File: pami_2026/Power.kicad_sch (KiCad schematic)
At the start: 6 parts, among them U2 AZ1117CH2-3.3, U3 AZ1117CH2-3.3

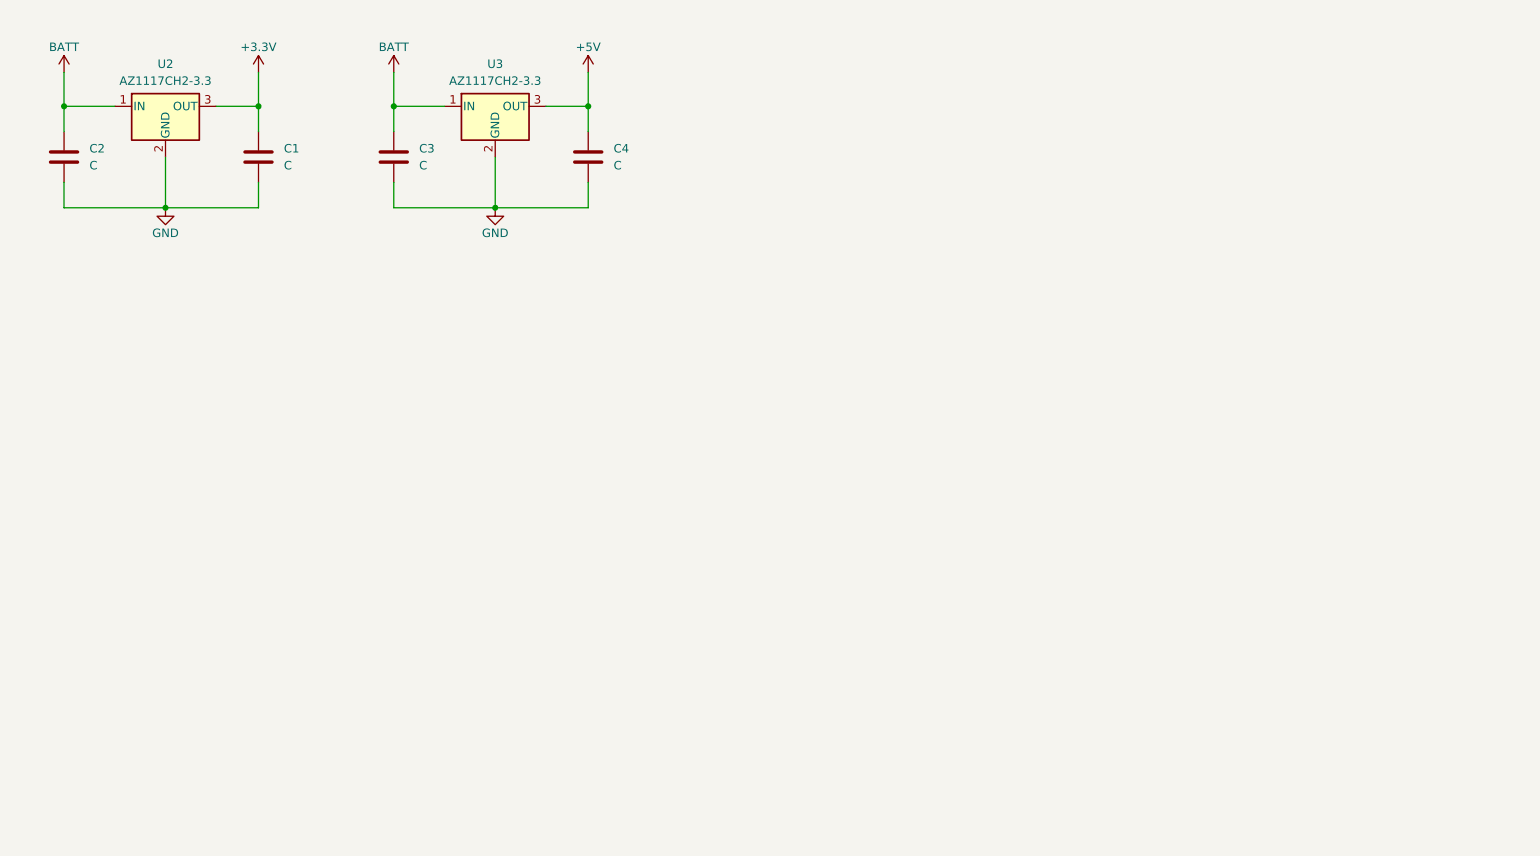
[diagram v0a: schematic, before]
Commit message: Battery circuit and DC Driver
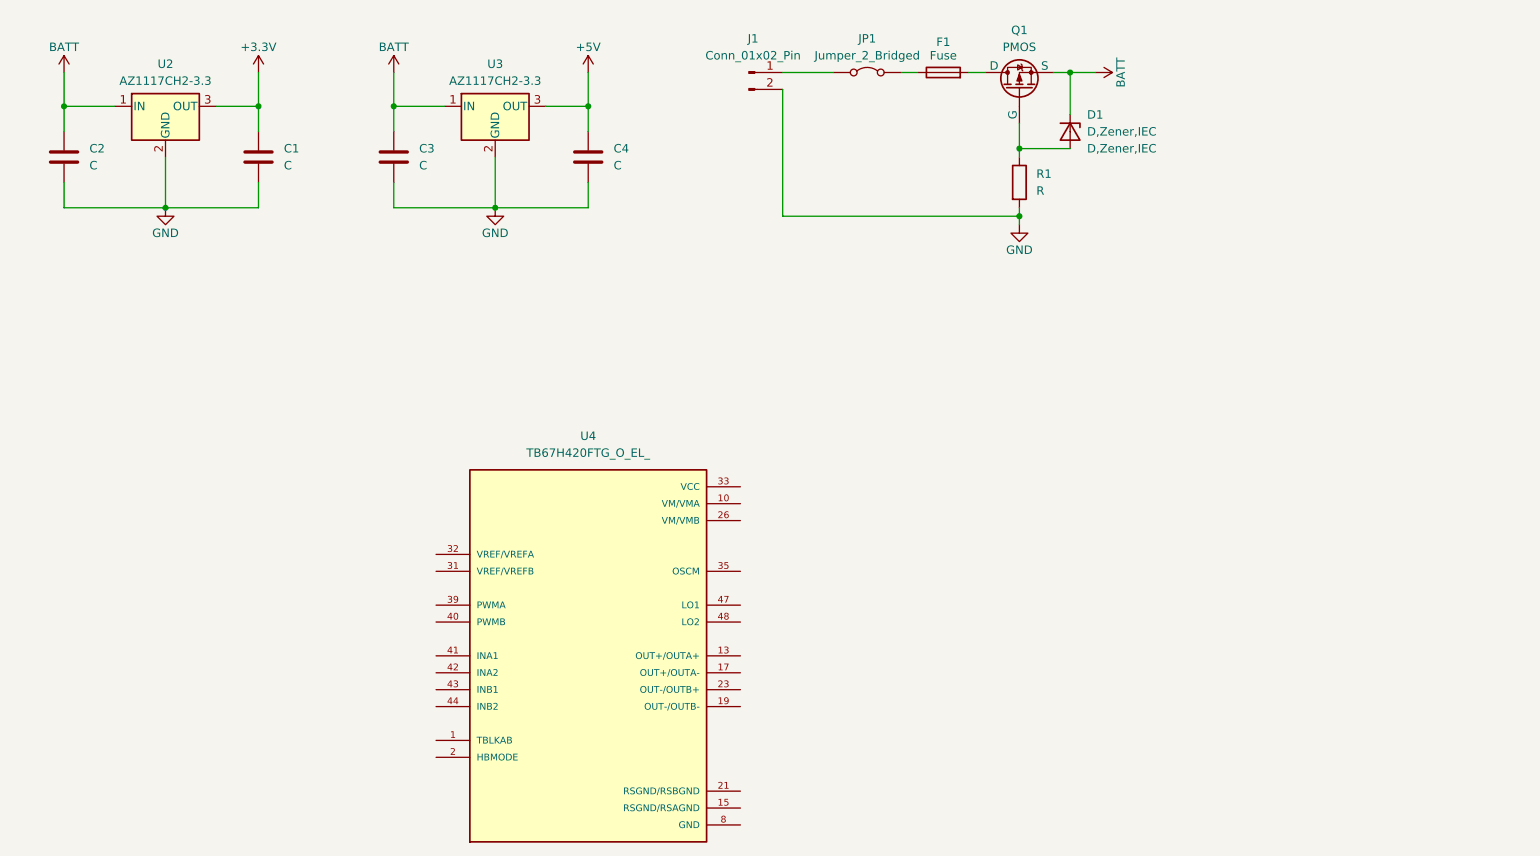
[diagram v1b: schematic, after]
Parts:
- added D1: ${SIM.PARAMS}, symbol PCM_Generic-50:D,Zener,IEC
- added F1: Fuse, symbol Device:Fuse
- added J1: Conn_01x02_Pin, symbol Connector:Conn_01x02_Pin
- added JP1: Jumper_2_Bridged, symbol Jumper:Jumper_2_Bridged
- added Q1: PMOS, symbol Simulation_SPICE:PMOS
- added R1: R, symbol Device:R
- added U4: TB67H420FTG_O_EL_, TB67H420FTG_O_EL_:IC_TB67H420FTG_O_EL_, symbol TB67H420FTG_O_EL_:TB67H420FTG_O_EL_
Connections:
- net BATT: now also D1.1 (K-), Q1.3 (S)
- net GND: now also J1.2 (Pin_2), R1.2, U4.29 (GND), U4.30 (GND), U4.49 (GND), U4.50 (GND), U4.51 (GND), U4.52 (GND), U4.53 (GND), U4.54 (GND), U4.55 (GND), U4.56 (GND), U4.57 (GND), U4.58 (GND), U4.59 (GND), U4.60 (GND), U4.61 (GND), U4.62 (GND), U4.63 (GND), U4.64 (GND), U4.65 (GND), U4.66 (GND), U4.67 (GND), U4.68 (GND), U4.69 (GND), U4.70 (GND), U4.71 (GND), U4.72 (GND), U4.73 (GND), U4.74 (GND), U4.75 (GND), U4.76 (GND), U4.77 (GND), U4.78 (GND), U4.79 (GND), U4.8 (GND), U4.80 (GND), U4.81 (GND), U4.82 (GND), U4.83 (GND), U4.84 (GND), U4.85 (GND), U4.86 (GND), U4.87 (GND), U4.88 (GND), U4.89 (GND), U4.90 (GND), U4.91 (GND), U4.92 (GND), U4.93 (GND), U4.94 (GND), U4.95 (GND), U4.96 (GND), U4.97 (GND), U4.98 (GND), U4.G1 (GND), U4.G2 (GND), U4.G3 (GND), U4.G4 (GND)
- new net: D1.2 (A+), Q1.2 (G), R1.1
- new net: F1.2, Q1.1 (D)
- new net: F1.1, JP1.2 (B)
- new net: J1.1 (Pin_1), JP1.1 (A)
- new net: U4.13 (OUT+/OUTA+), U4.14 (OUT+/OUTA+)
- new net: U4.17 (OUT+/OUTA-), U4.18 (OUT+/OUTA-)
- new net: U4.19 (OUT-/OUTB-), U4.20 (OUT-/OUTB-)
- new net: U4.23 (OUT-/OUTB+), U4.24 (OUT-/OUTB+)
- new net RSGND/RSAGND: U4.15 (RSGND/RSAGND), U4.16 (RSGND/RSAGND)
- new net RSGND/RSBGND: U4.21 (RSGND/RSBGND), U4.22 (RSGND/RSBGND)
- new net VCC: U4.33 (VCC), U4.34 (VCC)
- new net VM/VMA: U4.10 (VM/VMA), U4.11 (VM/VMA)
- new net VM/VMB: U4.26 (VM/VMB), U4.27 (VM/VMB)

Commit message: WIP alim stage
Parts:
- removed U2, U3: AZ1117CH2-3.3, Package_TO_SOT_SMD:SOT-223-3_TabPin2, symbol Regulator_Linear:AZ1117CH2-3.3
- added C5, C7, C8: 22µF, Capacitor_SMD:C_0201_0603Metric, symbol Device:C
- added C6: 100nF, Capacitor_SMD:C_0201_0603Metric, symbol Device:C
- added L1, L2: 4.7µH, Inductor_SMD_Wurth:L_Wurth_WE-LQSH-4020, symbol Device:L
- added U2: AP63205WU, Package_TO_SOT_SMD:TSOT-23-6, symbol Regulator_Switching:AP63205WU
- added U5: AP63203WU, Package_TO_SOT_SMD:TSOT-23-6, symbol Regulator_Switching:AP63203WU
- C1: value C -> 100nF; footprint (none) -> Capacitor_SMD:C_0201_0603Metric
- C2, C3: value C -> 10µF; footprint (none) -> Capacitor_SMD:C_0201_0603Metric
- C4: value C -> 22µF; footprint (none) -> Capacitor_SMD:C_0201_0603Metric
- R1: footprint (none) -> Resistor_SMD:R_0201_0603Metric
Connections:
- net RSGND/RSAGND is gone; now on net GND: U4.15 (RSGND/RSAGND), U4.16 (RSGND/RSAGND)
- net RSGND/RSBGND is gone; now on net GND: U4.21 (RSGND/RSBGND), U4.22 (RSGND/RSBGND)
- net VCC is gone; now on net +5V: U4.33 (VCC), U4.34 (VCC)
- net VM/VMA is gone; now on net BATT: U4.10 (VM/VMA), U4.11 (VM/VMA)
- net VM/VMB is gone; now on net BATT: U4.26 (VM/VMB), U4.27 (VM/VMB)
- net +3.3V: now also C4.1, C5.1, L1.2, U5.1 (FB); no longer C1.1
- net +5V: now also U4.31 (VREF/VREFB), U4.32 (VREF/VREFA), C7.1, C8.1, L2.2, U2.1 (FB); no longer C4.1
- net BATT: now also U2.2 (EN), U2.3 (IN), U5.2 (EN), U5.3 (IN)
- net GND: now also U4.1 (TBLKAB), U4.2 (HBMODE), U4.35 (OSCM), C5.2, C7.2, C8.2, U2.4 (GND), U5.4 (GND); no longer C1.2
- new net: C6.2, L2.1, U2.6 (BST)
- new net: C6.1, U2.5 (SW)
- new net: C1.1, U5.5 (SW)
- new net: C1.2, L1.1, U5.6 (BST)
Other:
- moved on the sheet: C3, C4, U4

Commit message: WIP actuators
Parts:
- added C10: C, symbol Device:C
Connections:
- net BATT: now also C10.2; no longer D1.1 (K-), Q1.3 (S)
- net DC_OUT_A+: now reaches U4.13 (OUT+/OUTA+), U4.14 (OUT+/OUTA+)
- net DC_OUT_A-: now reaches U4.17 (OUT+/OUTA-), U4.18 (OUT+/OUTA-)
- net DC_OUT_B-: now reaches U4.19 (OUT-/OUTB-), U4.20 (OUT-/OUTB-)
- net DC_OUT_B+: now reaches U4.23 (OUT-/OUTB+), U4.24 (OUT-/OUTB+)
- net PWM_A: now reaches U4.39 (PWMA)
- net PWM_B: now reaches U4.40 (PWMB)
- net DC_A1: now reaches U4.41 (INA1)
- net DC_A2: now reaches U4.42 (INA2)
- net DC_B1: now reaches U4.43 (INB1)
- net DC_B2: now reaches U4.44 (INB2)
- new net: C10.1, D1.1 (K-), Q1.3 (S)
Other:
- moved on the sheet: C2, C6, C7, C8, D1, F1, J1, JP1, L2, Q1, R1, U2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

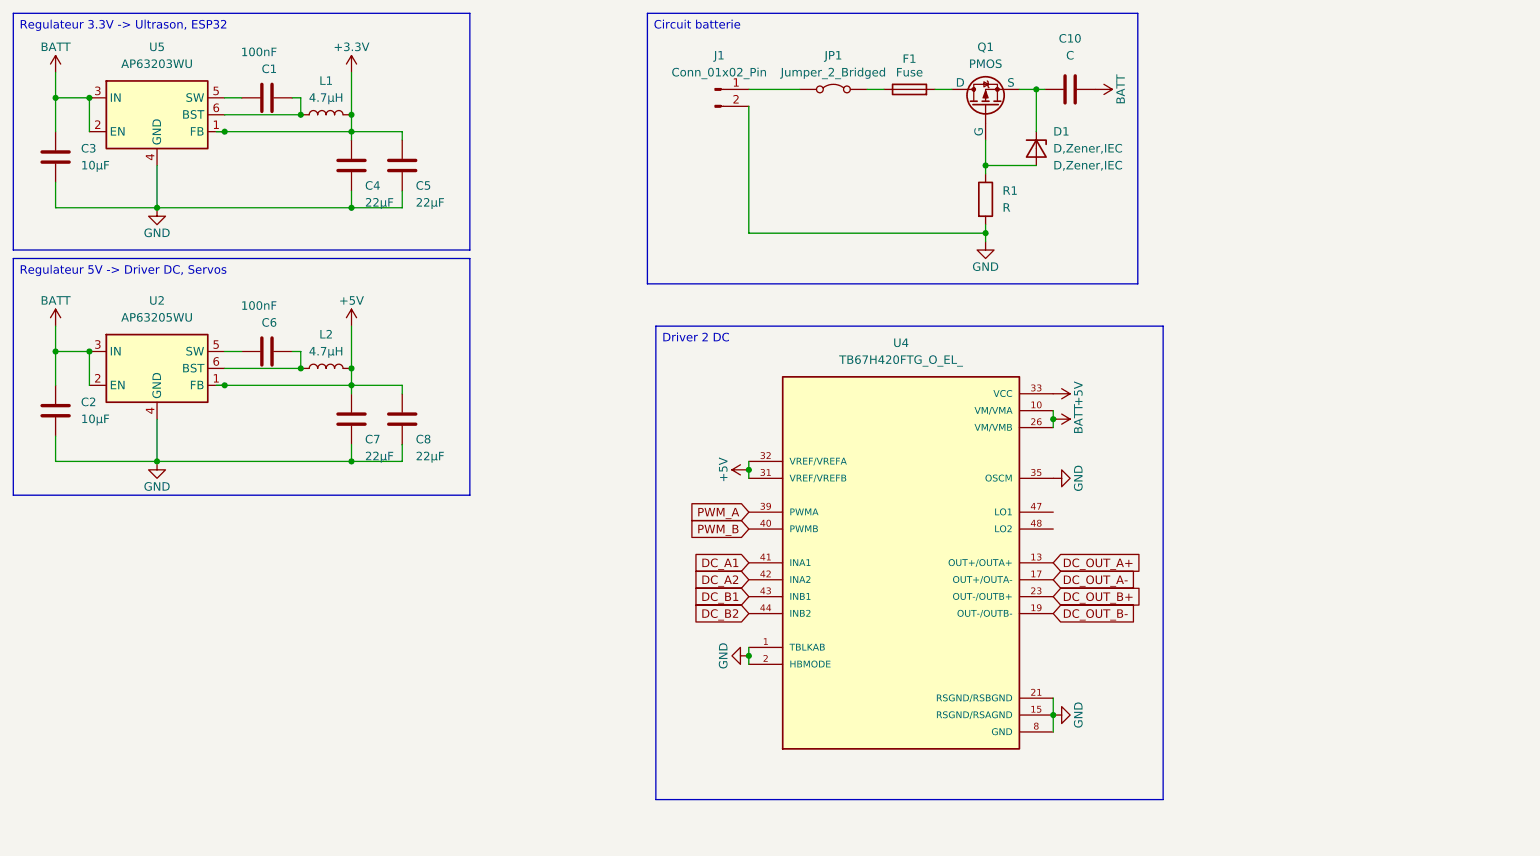
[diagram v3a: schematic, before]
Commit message: WIP USB programmer
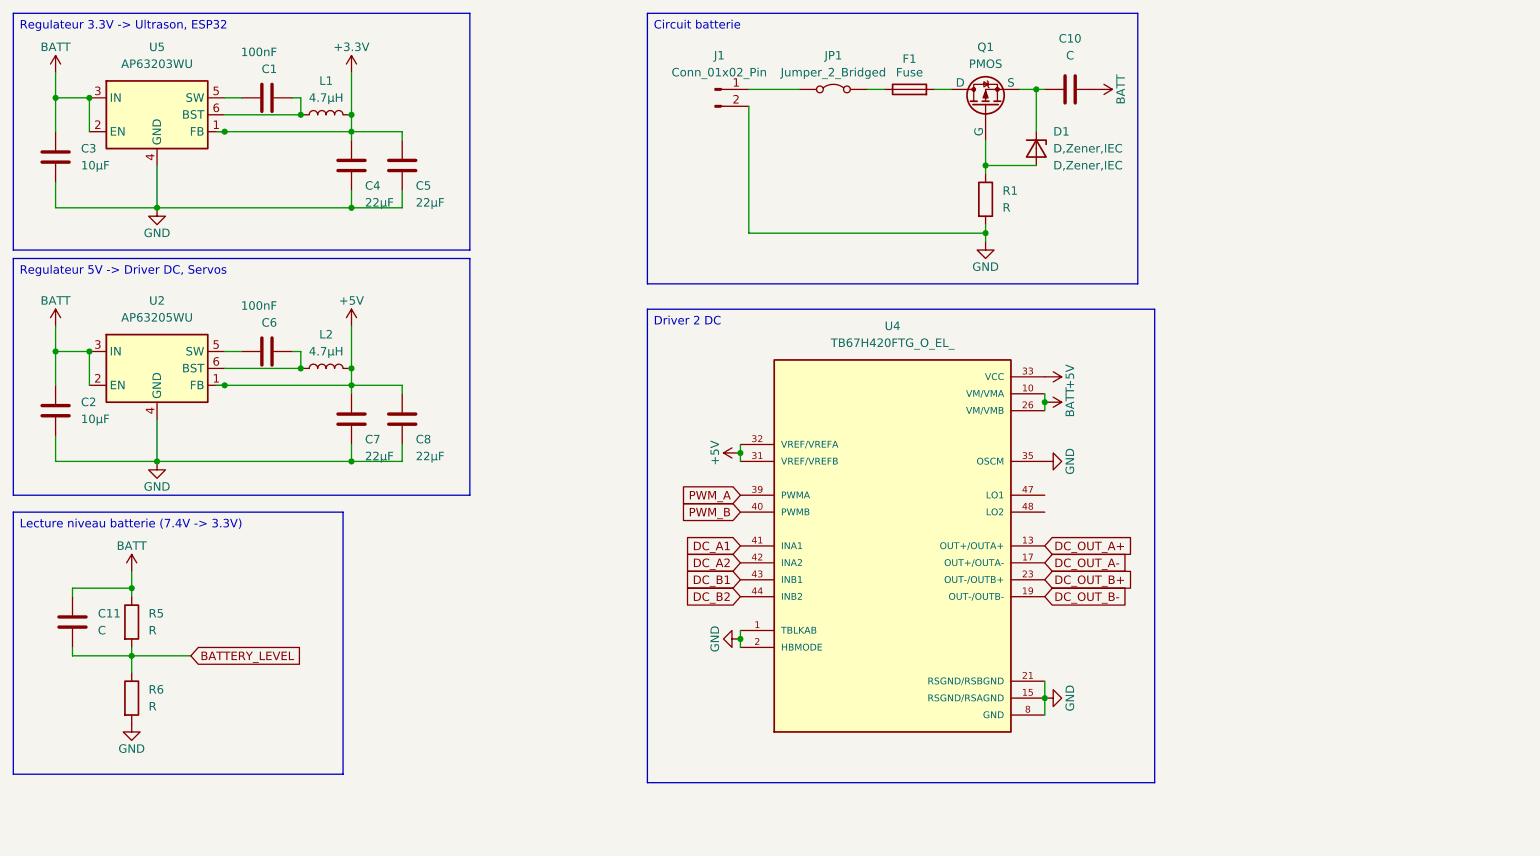
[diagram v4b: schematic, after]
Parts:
- added C11: C, symbol Device:C
- added R5, R6: R, symbol Device:R
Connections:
- net BATT: now also C11.1, R5.1
- net GND: now also R6.2
- new net BATTERY_LEVEL: C11.2, R5.2, R6.1
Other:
- moved on the sheet: U4

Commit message: Change DC drivers, apply datasheet recommendations, add big capacitor, remove USB programmer for simple connector
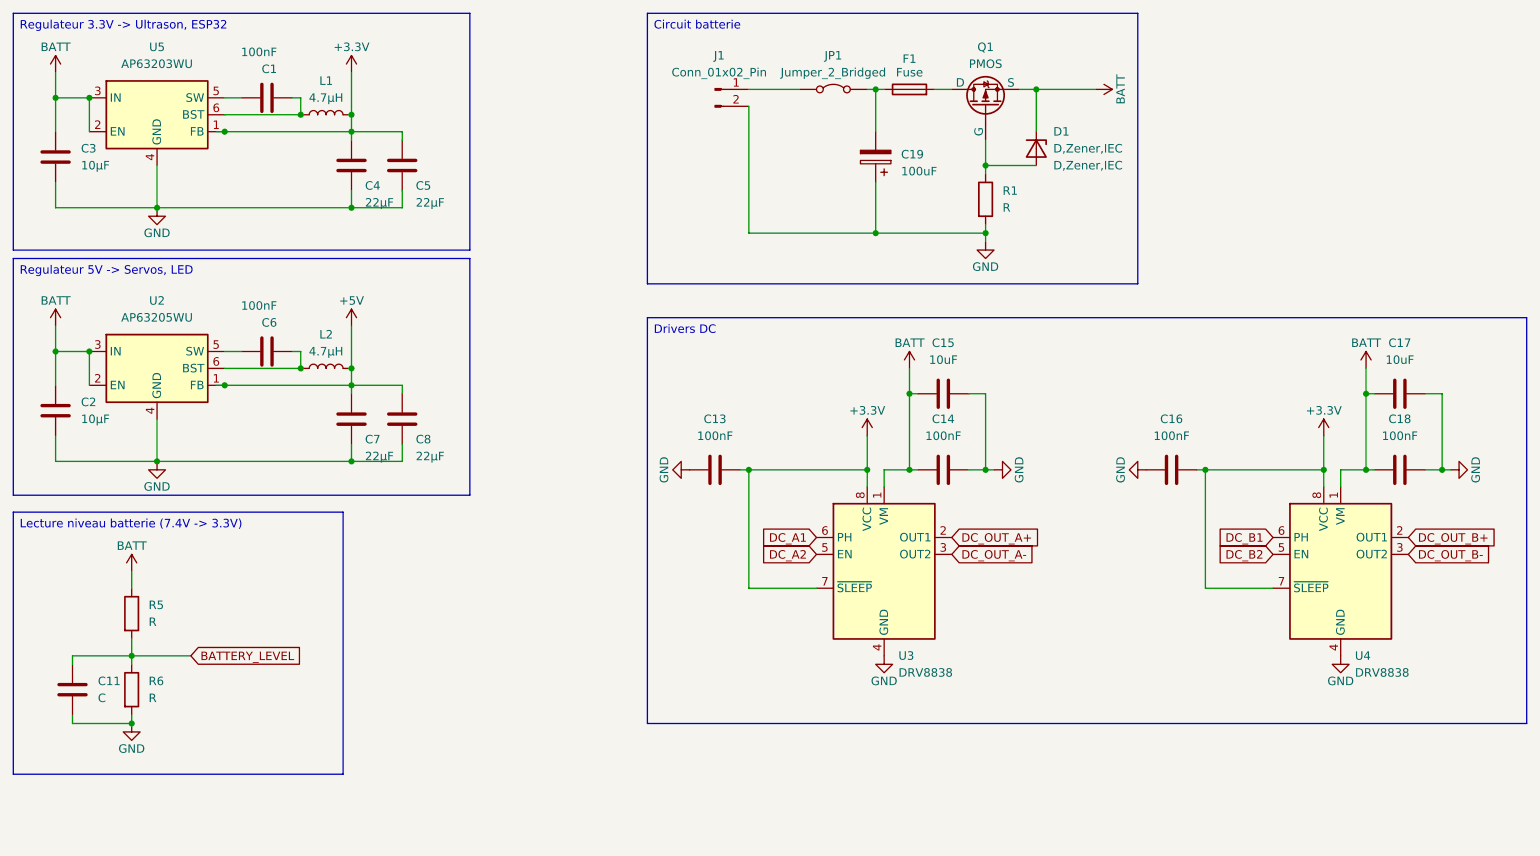
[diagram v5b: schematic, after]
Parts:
- removed C10: C, symbol Device:C
- removed U4: TB67H420FTG_O_EL_, TB67H420FTG_O_EL_:IC_TB67H420FTG_O_EL_, symbol TB67H420FTG_O_EL_:TB67H420FTG_O_EL_
- added C13, C14, C16, C18: 100nF, symbol Device:C
- added C15, C17: 10uF, symbol Device:C
- added C19: 100uF, symbol Device:C_Polarized
- added U3, U4: DRV8838, Package_SON:WSON-8-1EP_2x2mm_P0.5mm_EP0.9x1.6mm, symbol Driver_Motor:DRV8838
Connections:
- net +3.3V: now also C13.2, C16.2, U3.7 (~{SLEEP}), U3.8 (VCC), U4.7 (~{SLEEP}), U4.8 (VCC)
- net BATT: now also D1.1 (K-), Q1.3 (S), C14.1, C15.1, C17.1, C18.1, U3.1 (VM), U4.1 (VM); no longer C11.1
- net BATTERY_LEVEL: now also C11.1; no longer C11.2
- net DC_A1: now also U3.6 (PH)
- net DC_A2: now also U3.5 (EN)
- net DC_B1: now also U4.6 (PH)
- net DC_B2: now also U4.5 (EN)
- net DC_OUT_A+: now also U3.2 (OUT1)
- net DC_OUT_A-: now also U3.3 (OUT2)
- net DC_OUT_B+: now also U4.2 (OUT1)
- net DC_OUT_B-: now also U4.3 (OUT2)
- net GND: now also C11.2, C13.1, C14.2, C15.2, C16.1, C17.2, C18.2, C19.1, U3.4 (GND), U3.9 (GND), U4.4 (GND), U4.9 (GND)
- net at F1.1, JP1.2 (B): now also C19.2
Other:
- moved on the sheet: C11, R5, R6

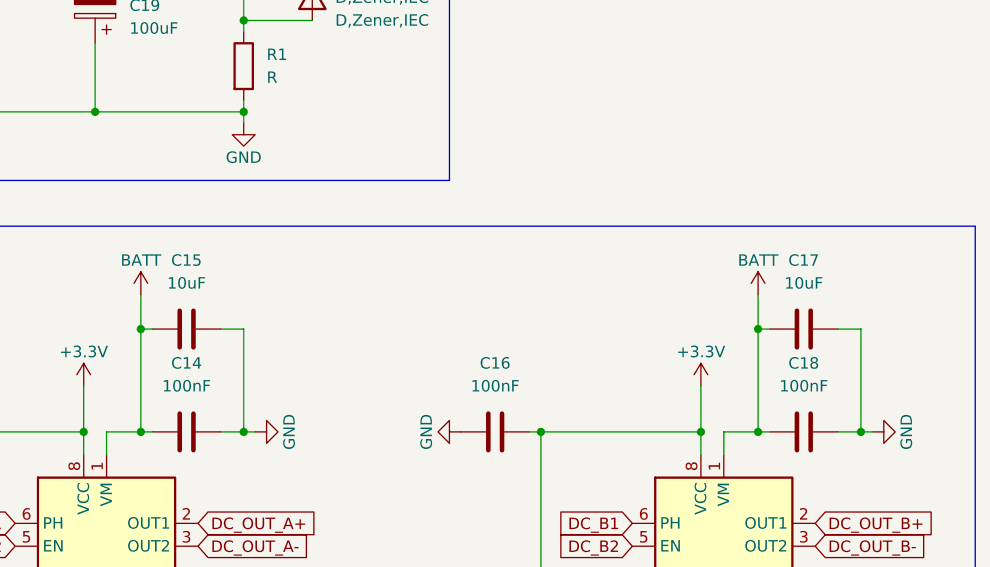
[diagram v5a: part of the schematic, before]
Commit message: Hall pull up
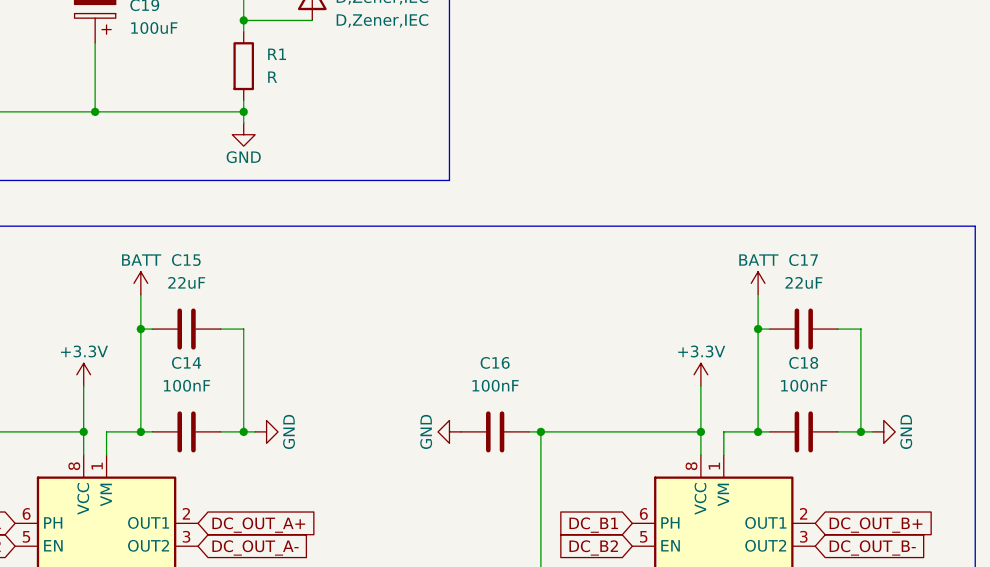
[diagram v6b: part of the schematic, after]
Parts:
- C15, C17: value 10uF -> 22uF
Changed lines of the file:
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@@
 			)
 		)
-		(property "Value" "10uF"
+		(property "Value" "22uF"
 			(at 156.21 74.93 90)
 			(effects
@@
 			)
 		)
-		(property "Value" "10uF"
+		(property "Value" "22uF"
 			(at 224.79 74.93 90)
 			(effects
